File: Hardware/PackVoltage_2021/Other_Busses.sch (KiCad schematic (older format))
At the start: 50 parts, among them Q10 PSMN025-80YL, Q6 PSMN025-80YL, Q7 PSMN025-80YL, Q8 PSMN025-80YL, Q9 PSMN025-80YL, U14 LT1910, U15 LT1910, U16 LT1910, U17 INA281, U18 INA281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

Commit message: changed mosfet footprint so its actually right
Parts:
- Q10, Q6, Q7, Q8, Q9: footprint Custom:LFPAK56_MOSFET -> Package_TO_SOT_SMD:LFPAK56
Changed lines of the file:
@@
 F 0 "Q8" H 3000 1450 50  0000 C CNN
 F 1 "PSMN025-80YL" H 3300 1350 50  0000 C CNN
-F 2 "Custom:LFPAK56_MOSFET" H 3200 1750 50  0001 C CNN
+F 2 "Package_TO_SOT_SMD:LFPAK56" H 3200 1750 50  0001 C CNN
 F 3 "~" H 3000 1650 50  0001 C CNN
 	1    3000 1650
@@
 F 0 "Q6" H 2950 3450 50  0000 C CNN
 F 1 "PSMN025-80YL" H 3250 3350 50  0000 C CNN
-F 2 "Custom:LFPAK56_MOSFET" H 3150 3750 50  0001 C CNN
+F 2 "Package_TO_SOT_SMD:LFPAK56" H 3150 3750 50  0001 C CNN
 F 3 "~" H 2950 3650 50  0001 C CNN
 	1    2950 3650
@@
 F 0 "Q7" H 2950 5650 50  0000 C CNN
 F 1 "PSMN025-80YL" H 3250 5550 50  0000 C CNN
-F 2 "Custom:LFPAK56_MOSFET" H 3150 5950 50  0001 C CNN
+F 2 "Package_TO_SOT_SMD:LFPAK56" H 3150 5950 50  0001 C CNN
 F 3 "~" H 2950 5850 50  0001 C CNN
 	1    2950 5850
@@
 F 0 "Q9" H 8350 1500 50  0000 C CNN
 F 1 "PSMN025-80YL" H 8650 1400 50  0000 C CNN
-F 2 "Custom:LFPAK56_MOSFET" H 8550 1800 50  0001 C CNN
+F 2 "Package_TO_SOT_SMD:LFPAK56" H 8550 1800 50  0001 C CNN
 F 3 "~" H 8350 1700 50  0001 C CNN
 	1    8350 1700
@@
 F 0 "Q10" H 8350 3550 50  0000 C CNN
 F 1 "PSMN025-80YL" H 8650 3450 50  0000 C CNN
-F 2 "Custom:LFPAK56_MOSFET" H 8550 3850 50  0001 C CNN
+F 2 "Package_TO_SOT_SMD:LFPAK56" H 8550 3850 50  0001 C CNN
 F 3 "~" H 8350 3750 50  0001 C CNN
 	1    8350 3750

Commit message: updated mosfet footprints
but for real this time
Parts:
- Q10, Q6, Q7, Q8, Q9: value PSMN025-80YL -> BUK7M8R5-40HX; footprint Package_TO_SOT_SMD:LFPAK56 -> Package_TO_SOT_SMD:LFPAK33; symbol Device:Q_NMOS_DGS -> Transistor_FET:BUK9M24-40EX
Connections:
- net at C26.1, F8.2, U16.6 (SENSE)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: now also Q8.5 (D); no longer Q8.1 (D)
- net at Q8.2 (S): now also Q8.1 (S), Q8.3 (S), R24.1, R27.1, U19.3 (+); no longer U16.5 (GATE)
- net at C25.1, F7.2, U15.6 (SENSE)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: now also Q7.5 (D); no longer Q7.1 (D)
- net at Q7.3 (S), R23.1, R26.1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: now also Q7.1 (S), Q7.2 (S)
- net at U15.5 (GATE): now also Q7.4 (G); no longer Q7.2 (G)
- net at C29.1, F9.2, U20.6 (SENSE)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: now also Q9.5 (D); no longer Q9.1 (D)
- net at Q9.2 (S): now also Q9.1 (S), Q9.3 (S), R30.1, U22.3 (+); no longer U20.5 (GATE)
- net at C30.1, F10.2, U21.6 (SENSE)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: now also Q10.5 (D); no longer Q10.1 (D)
- net at Q10.2 (S): now also Q10.1 (S), Q10.3 (S), R31.1, R33.1, U23.3 (+); no longer U21.5 (GATE)
- net at C24.1, F6.2, U14.6 (SENSE)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: now also Q6.5 (D); no longer Q6.1 (D)
- net at Q6.2 (S): now also Q6.1 (S), Q6.3 (S), R22.1, R25.1, U17.3 (+); no longer U14.5 (GATE)
- new net: Q8.4 (G), U16.5 (GATE)
- new net: Q9.4 (G), U20.5 (GATE)
- new net: Q10.4 (G), U21.5 (GATE)
- new net: Q6.4 (G), U14.5 (GATE)
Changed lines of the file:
@@
 Motor Busses
 $Comp
-L Device:Q_NMOS_DGS Q?
+L Transistor_FET:BUK9M24-40EX Q?
 U 1 1 5F768EE8
 P 3000 1650
@@
 AR Path="/5F8EFCC9/5F768EE8" Ref="Q8"  Part="1"
 F 0 "Q8" H 3000 1450 50  0000 C CNN
-F 1 "PSMN025-80YL" H 3300 1350 50  0000 C CNN
-F 2 "Package_TO_SOT_SMD:LFPAK56" H 3200 1750 50  0001 C CNN
+F 1 "BUK7M8R5-40HX" H 3300 1350 50  0000 C CNN
+F 2 "Package_TO_SOT_SMD:LFPAK33" H 3200 1750 50  0001 C CNN
 F 3 "~" H 3000 1650 50  0001 C CNN
 	1    3000 1650
@@
 	3750 2100 4000 2100
 $Comp
-L Device:Q_NMOS_DGS Q?
+L Transistor_FET:BUK9M24-40EX Q?
 U 1 1 5F9AF794
 P 2950 3650
@@
 AR Path="/5F8EFCC9/5F9AF794" Ref="Q6"  Part="1"
 F 0 "Q6" H 2950 3450 50  0000 C CNN
-F 1 "PSMN025-80YL" H 3250 3350 50  0000 C CNN
-F 2 "Package_TO_SOT_SMD:LFPAK56" H 3150 3750 50  0001 C CNN
+F 1 "BUK7M8R5-40HX" H 3250 3350 50  0000 C CNN
+F 2 "Package_TO_SOT_SMD:LFPAK33" H 3150 3750 50  0001 C CNN
 F 3 "~" H 2950 3650 50  0001 C CNN
 	1    2950 3650
@@
 Current_Sensor_T1
 $Comp
-L Device:Q_NMOS_DGS Q?
+L Transistor_FET:BUK9M24-40EX Q?
 U 1 1 5F9AF7A1
 P 2950 5850
@@
 AR Path="/5F8EFCC9/5F9AF7A1" Ref="Q7"  Part="1"
 F 0 "Q7" H 2950 5650 50  0000 C CNN
-F 1 "PSMN025-80YL" H 3250 5550 50  0000 C CNN
-F 2 "Package_TO_SOT_SMD:LFPAK56" H 3150 5950 50  0001 C CNN
+F 1 "BUK7M8R5-40HX" H 3250 5550 50  0000 C CNN
+F 2 "Package_TO_SOT_SMD:LFPAK33" H 3150 5950 50  0001 C CNN
 F 3 "~" H 2950 5850 50  0001 C CNN
 	1    2950 5850
@@
 Current_Sensor_V1
 $Comp
-L Device:Q_NMOS_DGS Q?
+L Transistor_FET:BUK9M24-40EX Q?
 U 1 1 5F8B2B16
 P 8350 1700
@@
 AR Path="/5F8EFCC9/5F8B2B16" Ref="Q9"  Part="1"
 F 0 "Q9" H 8350 1500 50  0000 C CNN
-F 1 "PSMN025-80YL" H 8650 1400 50  0000 C CNN
-F 2 "Package_TO_SOT_SMD:LFPAK56" H 8550 1800 50  0001 C CNN
+F 1 "BUK7M8R5-40HX" H 8650 1400 50  0000 C CNN
+F 2 "Package_TO_SOT_SMD:LFPAK33" H 8550 1800 50  0001 C CNN
 F 3 "~" H 8350 1700 50  0001 C CNN
 	1    8350 1700
@@
 Anderson_D1
 $Comp
-L Device:Q_NMOS_DGS Q?
+L Transistor_FET:BUK9M24-40EX Q?
 U 1 1 5F8E41E6
 P 8350 3750
@@
 AR Path="/5F8EFCC9/5F8E41E6" Ref="Q10"  Part="1"
 F 0 "Q10" H 8350 3550 50  0000 C CNN
-F 1 "PSMN025-80YL" H 8650 3450 50  0000 C CNN
-F 2 "Package_TO_SOT_SMD:LFPAK56" H 8550 3850 50  0001 C CNN
+F 1 "BUK7M8R5-40HX" H 8650 3450 50  0000 C CNN
+F 2 "Package_TO_SOT_SMD:LFPAK33" H 8550 3850 50  0001 C CNN
 F 3 "~" H 8350 3750 50  0001 C CNN
 	1    8350 3750

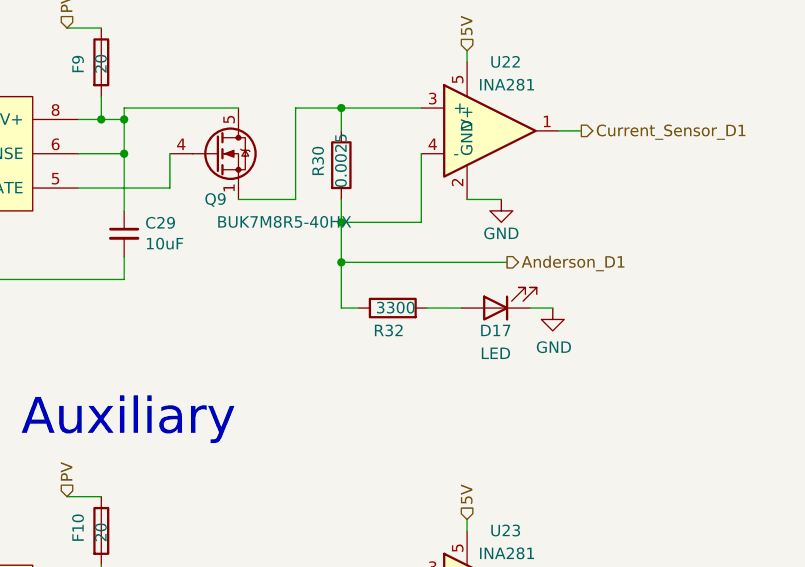
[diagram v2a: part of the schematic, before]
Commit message: uhh more circuits
finished top circuits on layout, fixed two resistors in schematic
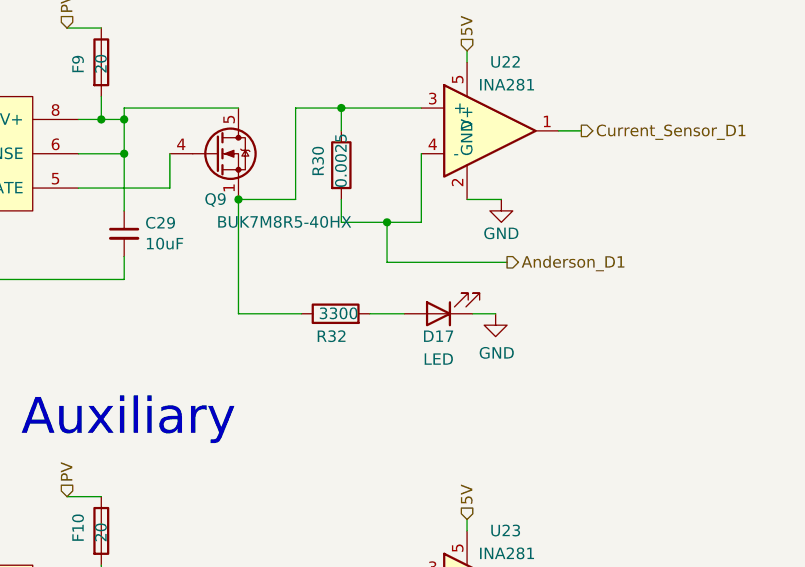
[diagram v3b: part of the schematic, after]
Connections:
- net Anderson_D1: no longer R32.1
- net at Q9.1 (S), Q9.2 (S), Q9.3 (S)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: now also R32.1
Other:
- moved on the sheet: D17, R32
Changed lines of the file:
@@
 L Device:LED D?
 U 1 1 5F8B2B79
-P 9575 2375
+P 9325 2400
 AR Path="/5F7A6A8B/5F8B2B79" Ref="D?"  Part="1"
 AR Path="/5F8EFCC9/5F8B2B79" Ref="D17"  Part="1"
-F 0 "D17" H 9575 2475 50  0000 C CNN
-F 1 "LED" H 9575 2575 50  0000 C CNN
-F 2 "LED_SMD:LED_0603_1608Metric_Pad1.05x0.95mm_HandSolder" H 9575 2375 50  0001 C CNN
-F 3 "~" H 9575 2375 50  0001 C CNN
-	1    9575 2375
+F 0 "D17" H 9325 2500 50  0000 C CNN
+F 1 "LED" H 9325 2600 50  0000 C CNN
+F 2 "LED_SMD:LED_0603_1608Metric_Pad1.05x0.95mm_HandSolder" H 9325 2400 50  0001 C CNN
+F 3 "~" H 9325 2400 50  0001 C CNN
+	1    9325 2400
 	-1   0    0    1
 $EndComp
@@
 L Device:R R?
 U 1 1 5F9AF7B7
-P 9125 2375
+P 8875 2400
 AR Path="/5F7A6A8B/5F9AF7B7" Ref="R?"  Part="1"
 AR Path="/5F8EFCC9/5F9AF7B7" Ref="R32"  Part="1"
-F 0 "R32" V 9025 2325 50  0000 L CNN
-F 1 "3300" V 9125 2275 50  0000 L CNN
-F 2 "Resistor_SMD:R_0603_1608Metric_Pad1.05x0.95mm_HandSolder" V 9055 2375 50  0001 C CNN
-F 3 "~" H 9125 2375 50  0001 C CNN
-	1    9125 2375
+F 0 "R32" V 8775 2350 50  0000 L CNN
+F 1 "3300" V 8875 2300 50  0000 L CNN
+F 2 "Resistor_SMD:R_0603_1608Metric_Pad1.05x0.95mm_HandSolder" V 8805 2400 50  0001 C CNN
+F 3 "~" H 8875 2400 50  0001 C CNN
+	1    8875 2400
 	0    -1   -1   0
 $EndComp
 Wire Wire Line
-	9275 2375 9425 2375
-Wire Wire Line
-	9725 2375 9825 2375
+	9025 2400 9175 2400
+Wire Wire Line
+	9475 2400 9575 2400
 Text HLabel 7700 1150 1    50   Input ~ 0
 PV
@@
 L power:GND #PWR?
 U 1 1 5F9AF7BA
-P 9825 2375
+P 9575 2400
 AR Path="/5F7A6A8B/5F9AF7BA" Ref="#PWR?"  Part="1"
 AR Path="/5F8EFCC9/5F9AF7BA" Ref="#PWR059"  Part="1"
-F 0 "#PWR059" H 9825 2125 50  0001 C CNN
-F 1 "GND" H 9830 2202 50  0000 C CNN
-F 2 "" H 9825 2375 50  0001 C CNN
-F 3 "" H 9825 2375 50  0001 C CNN
-	1    9825 2375
+F 0 "#PWR059" H 9575 2150 50  0001 C CNN
+F 1 "GND" H 9580 2227 50  0000 C CNN
+F 2 "" H 9575 2400 50  0001 C CNN
+F 3 "" H 9575 2400 50  0001 C CNN
+	1    9575 2400
 	1    0    0    -1
 $EndComp
@@
 	8450 3950 8450 4400
 Wire Wire Line
-	8900 2175 8900 2375
-Wire Wire Line
-	8900 2375 8975 2375
-Wire Wire Line
-	8900 2175 9625 2175
-Wire Wire Line
-	8900 2000 9250 2000
-Wire Wire Line
-	8900 2000 8900 2175
-Connection ~ 8900 2000
-Connection ~ 8900 2175
+	8900 2000 9100 2000
+Wire Wire Line
+	9100 2000 9100 2175
+Connection ~ 8450 1900
+Connection ~ 9100 2000
+Wire Wire Line
+	9100 2000 9250 2000
+Wire Wire Line
+	9100 2175 9625 2175
+Wire Wire Line
+	8450 1900 8450 2400
+Wire Wire Line
+	8450 2400 8725 2400
 $EndSCHEMATC
